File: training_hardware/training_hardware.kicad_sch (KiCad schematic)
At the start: 0 parts

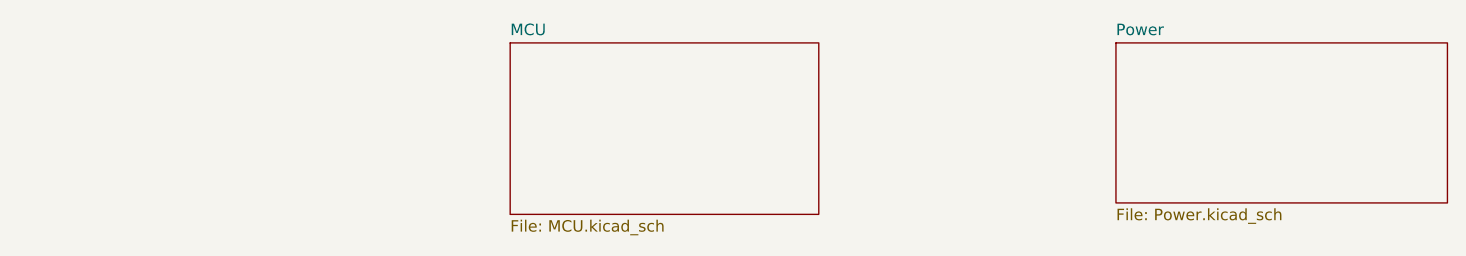
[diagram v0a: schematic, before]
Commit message: Add Ethernet
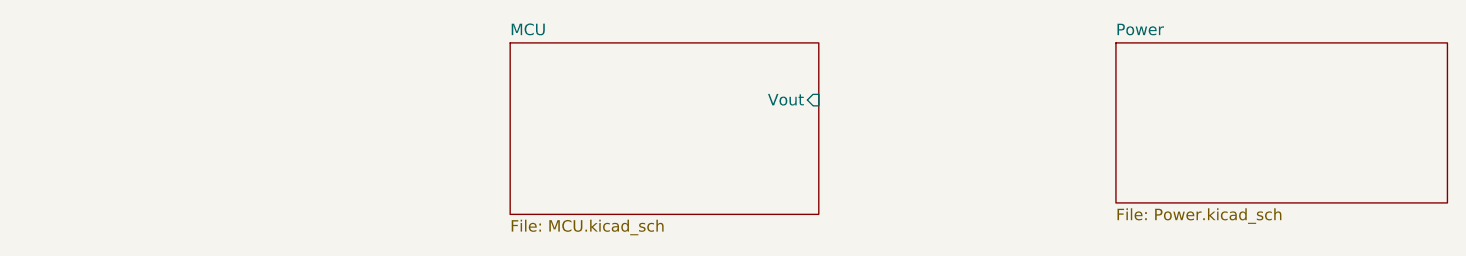
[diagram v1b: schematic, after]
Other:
- sheet MCU ports: added Vout; removed none
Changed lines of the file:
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@@
+			)
+		)
+		(pin "Vout" input
+			(at 148.59 90.17 0)
+			(effects
+				(font
+					(size 1.27 1.27)
+				)
+				(justify right)
 			)
 		)

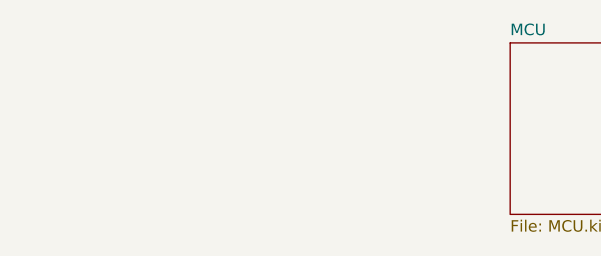
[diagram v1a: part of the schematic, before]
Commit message: Add CAN Transciever
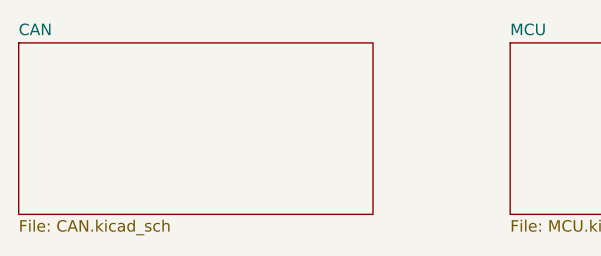
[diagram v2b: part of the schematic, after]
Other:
- added sheet CAN (CAN.kicad_sch)
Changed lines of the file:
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@@
+		)
+	)
+	(sheet
+		(at 59.69 83.82)
+		(size 39.37 19.05)
+		(exclude_from_sim no)
+		(in_bom yes)
+		(on_board yes)
+		(dnp no)
+		(fields_autoplaced yes)
+		(stroke
+			(width 0.1524)
+			(type solid)
+		)
+		(fill
+			(color 0 0 0 0.0000)
+		)
+		(property "Sheetname" "CAN"
+			(at 59.69 83.1084 0)
+			(effects
+				(font
+					(size 1.27 1.27)
+				)
+				(justify left bottom)
+			)
+		)
+		(property "Sheetfile" "CAN.kicad_sch"
+			(at 59.69 103.4546 0)
+			(effects
+				(font
+					(size 1.27 1.27)
+				)
+				(justify left top)
+			)
+		)
+		(instances
+			(project "training_hardware"
+				(path "/19aa0e78-5ab4-46df-84c9-9ca161187559"
+					(page "4")
+				)
+			)
 		)
 	)

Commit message: Finnish Schematic
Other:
- sheet CAN ports: added RXD, STBY, TXD; removed none
- sheet MCU ports: added CRX1, CTX1, STBY; removed Vout
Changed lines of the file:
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@@
 	(generator_version "9.0")
 	(paper "A4")
+	(wire
+		(pts
+			(xy 99.06 91.44) (xy 114.3 91.44)
+		)
+		(stroke
+			(width 0)
+			(type default)
+		)
+	)
+	(wire
+		(pts
+			(xy 99.06 88.9) (xy 114.3 88.9)
+		)
+		(stroke
+			(width 0)
+			(type default)
+		)
+	)
+	(wire
+		(pts
+			(xy 99.06 93.98) (xy 114.3 93.98)
+		)
+		(stroke
+			(width 0)
+			(type default)
+		)
+	)
 	(sheet
 		(at 181.61 83.82)
@@
 			)
 		)
-		(pin "Vout" input
-			(at 148.59 90.17 0)
+		(pin "CRX1" input
+			(at 114.3 88.9 180)
 			(effects
 				(font
 					(size 1.27 1.27)
 				)
-				(justify right)
+				(justify left)
+			)
+		)
+		(pin "CTX1" output
+			(at 114.3 93.98 180)
+			(effects
+				(font
+					(size 1.27 1.27)
+				)
+				(justify left)
+			)
+		)
+		(pin "STBY" output
+			(at 114.3 91.44 180)
+			(effects
+				(font
+					(size 1.27 1.27)
+				)
+				(justify left)
 			)
 		)
@@
 			)
 		)
+		(pin "RXD" output
+			(at 99.06 88.9 0)
+			(effects
+				(font
+					(size 1.27 1.27)
+				)
+				(justify right)
+			)
+		)
+		(pin "STBY" input
+			(at 99.06 91.44 0)
+			(effects
+				(font
+					(size 1.27 1.27)
+				)
+				(justify right)
+			)
+		)
+		(pin "TXD" input
+			(at 99.06 93.98 0)
+			(effects
+				(font
+					(size 1.27 1.27)
+				)
+				(justify right)
+			)
+		)
